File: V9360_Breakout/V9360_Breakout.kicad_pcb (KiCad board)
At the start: 2 copper layers, 1 part

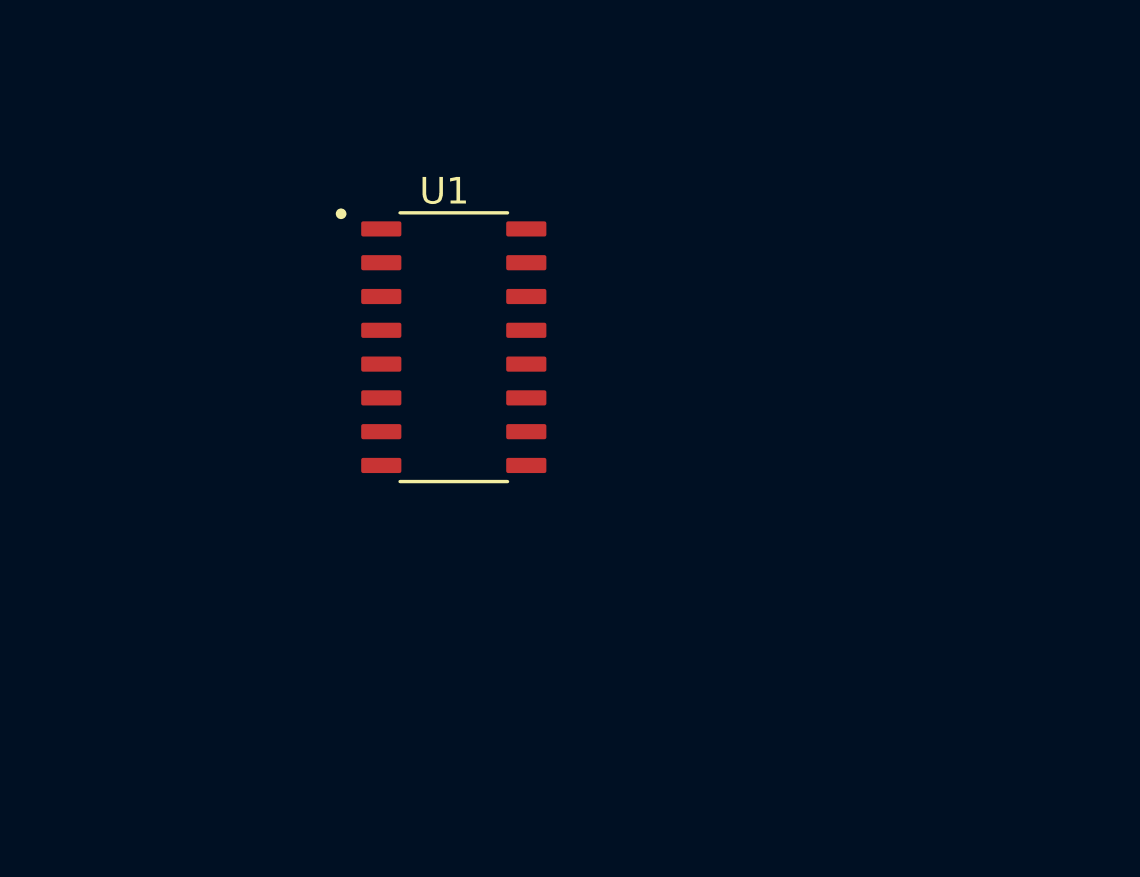
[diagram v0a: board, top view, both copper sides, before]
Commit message: Add routing and filters
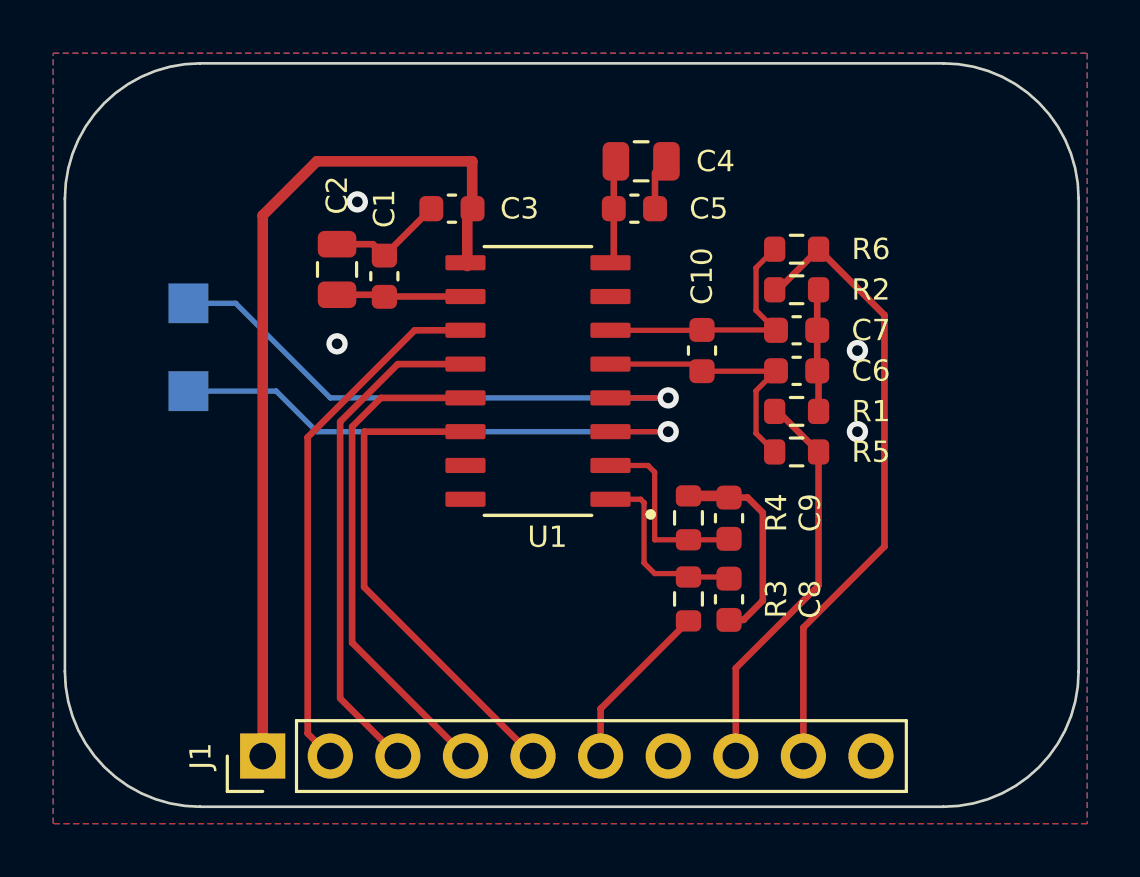
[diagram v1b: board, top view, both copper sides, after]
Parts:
- added C1: 100n, Capacitor_SMD:C_0603_1608Metric, F.Cu at (132.8, 90.4)
- added C10: 100p, Capacitor_SMD:C_0603_1608Metric, F.Cu at (144.8, 93.2)
- added C2: 4.7u, Capacitor_SMD:C_0805_2012Metric, F.Cu at (131.1, 90.2)
- added C3: 100n, Capacitor_SMD:C_0603_1608Metric, F.Cu at (135.4, 87.9)
- added C4: 4.7u, Capacitor_SMD:C_0805_2012Metric, F.Cu at (142.5, 86.1)
- added C5: 100n, Capacitor_SMD:C_0603_1608Metric, F.Cu at (142.2, 87.9)
- added C6: 33n, Capacitor_SMD:C_0603_1608Metric, F.Cu at (148.3, 94.0)
- added C7: 33n, Capacitor_SMD:C_0603_1608Metric, F.Cu at (148.3, 92.5)
- added C8: 33n, Capacitor_SMD:C_0603_1608Metric, F.Cu at (145.8, 102.6)
- added C9: 33n, Capacitor_SMD:C_0603_1608Metric, F.Cu at (145.8, 99.5)
- added J1: Conn_01x10_Pin, Connector_PinHeader_2.54mm:PinHeader_1x10_P2.54mm_Vertical, F.Cu at (128.3, 108.5)
- added R1: 2R2, Resistor_SMD:R_0603_1608Metric, F.Cu at (148.3, 95.5)
- added R2: 2R2, Resistor_SMD:R_0603_1608Metric, F.Cu at (148.3, 90.9)
- added R3: 1k, Resistor_SMD:R_0603_1608Metric, F.Cu at (144.3, 102.6)
- added R4: 1k, Resistor_SMD:R_0603_1608Metric, F.Cu at (144.3, 99.5)
- added R5: 1k, Resistor_SMD:R_0603_1608Metric, F.Cu at (148.3, 97.0)
- added R6: 1k, Resistor_SMD:R_0603_1608Metric, F.Cu at (148.3, 89.4)
- added TP1: TestPoint, TestPoint:TestPoint_Pad_1.5x1.5mm, B.Cu at (125.5, 91.4)
- added TP2: TestPoint, TestPoint:TestPoint_Pad_1.5x1.5mm, B.Cu at (125.5, 94.7)
- U1: value ~ -> V9360
- moved U1 3.41 mm to (138.6, 94.4), turned to 180 degrees
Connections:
- U1 pad 1: unconnected-(U1-UP-Pad1) -> UP
- U1 pad 10: unconnected-(U1-DVCC-Pad10) -> Net-(U1-DVCC)
- U1 pad 11: unconnected-(U1-P3-Pad11) -> P3
- U1 pad 12: unconnected-(U1-P2-Pad12) -> P2
- U1 pad 13: unconnected-(U1-RX-Pad13) -> RX
- U1 pad 14: unconnected-(U1-TX-Pad14) -> TX
- U1 pad 2: unconnected-(U1-UN-Pad2) -> UN
- U1 pad 3: unconnected-(U1-IBN-Pad3) -> IBN
- U1 pad 4: unconnected-(U1-IBP-Pad4) -> IBP
- U1 pad 5: unconnected-(U1-IAN-Pad5) -> IAN
- U1 pad 6: unconnected-(U1-IAP-Pad6) -> IAP
- U1 pad 7: unconnected-(U1-VSS-Pad7) -> UN_IN
- U1 pad 8: unconnected-(U1-VREF-Pad8) -> Net-(U1-VREF)
- U1 pad 9: unconnected-(U1-VDD-Pad9) -> VIN
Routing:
- net VIN: track 0.00 -> 33.1 mm
- net IAP_IN: track 0.00 -> 23.6 mm
- net IBP: track 0.00 -> 21.9 mm, vias 0 -> 1
- net IBN: track 0.00 -> 21.0 mm, vias 0 -> 1
- net P3: track 0.00 -> 19.9 mm
- net P2: track 0.00 -> 19.3 mm
- net UN_IN: track 0.00 -> 18.9 mm, vias 0 -> 4
- net RX: track 0.00 -> 18.9 mm
- net TX: track 0.00 -> 18.8 mm
- net IAN_IN: track 0.00 -> 15.0 mm
- net IAP: track 0.00 -> 10.1 mm
- net IAN: track 0.00 -> 9.99 mm
- net UN: track 0.00 -> 7.12 mm
- net UP: track 0.00 -> 7.02 mm
- net UP_IN: track 0.00 -> 6.45 mm
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- added copper zone on B.Cu, net UN_IN
- added copper zone on F.Cu, net UN_IN
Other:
- board outline added: 38.1 x 27.9 mm

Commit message: Add silk screen refinements
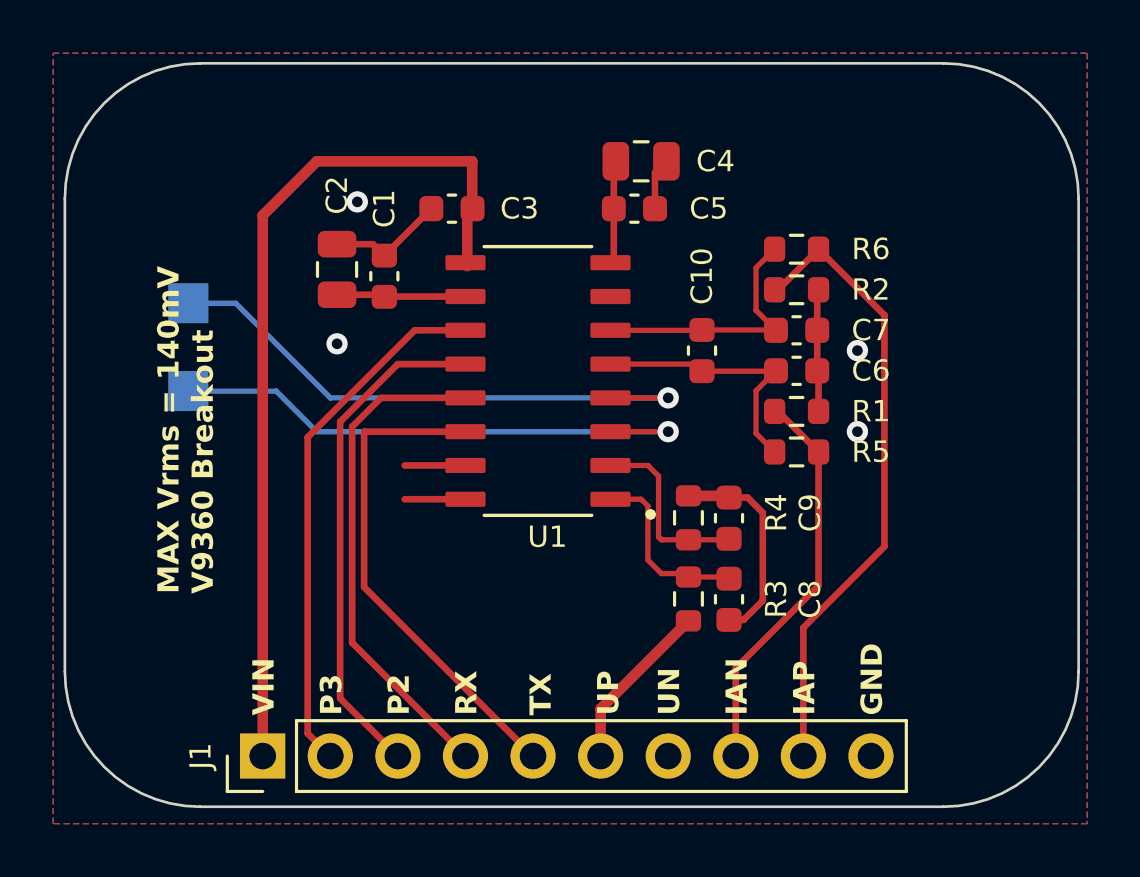
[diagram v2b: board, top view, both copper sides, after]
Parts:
- added SYM1: Logo_Open_Hardware_Small, Symbol:OSHW-Logo2_9.8x8mm_SilkScreen, B.Cu at (139.7, 95.8)
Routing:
- net unconnected-(U1-NC-Pad16): track 0.00 -> 2.29 mm
- net unconnected-(U1-CTI-Pad15): track 0.00 -> 2.29 mm
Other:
- board text added: "GND"
- board text added: "IAN"
- board text added: "IAP"
- board text added: "MAX Vrms = 140mV V9360 Breakout"
- board text added: "P2"
- board text added: "P3"
- board text added: "RX"
- board text added: "TX"
- board text added: "UN"
- board text added: "UP"
- board text added: "VIN"
- board text added: "by Tisham Dhar https://whatnick.com v0.1 27/12/2024"

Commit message: Add Gerbers and BOM
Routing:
- net UN_IN: vias 4 -> 17
